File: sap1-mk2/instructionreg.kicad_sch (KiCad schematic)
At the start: 0 parts

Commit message: added A Register, B Register, Instruction Register, and Memory Address Register
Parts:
- added C18, C19, C20: 0.1μF, symbol Device:C_Small
- added D18, D19, D20, D21: BLUE, symbol Device:LED
- added D22, D23, D24, D25: YELLOW, symbol Device:LED
- added R24, R25, R26, R27, R28, R29, R30, R31: 220, symbol Device:R
- added U13: 74LS245, symbol 74xx:74LS245
- added U14, U15: 74LS173, symbol 74xx:74LS173
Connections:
- new net: D21.1 (K), R27.1
- new net: D21.2 (A), U13.2 (A0), U15.3 (Q0)
- new net: D20.2 (A), U13.3 (A1), U15.4 (Q1)
- new net: D19.2 (A), U13.4 (A2), U15.5 (Q2)
- new net: D18.2 (A), U13.5 (A3), U15.6 (Q3)
- new net: D18.1 (K), R24.1
- new net: D22.1 (K), R28.1
- new net: D25.1 (K), R31.1
- new net: D19.1 (K), R25.1
- new net: D24.1 (K), R30.1
- new net: D23.1 (K), R29.1
- new net: D20.1 (K), R26.1
- new net +5V: C18.2, C19.2, C20.2, U13.1 (A->B), U13.20 (VCC), U14.16 (VCC), U15.16 (VCC)
- new net BUS_0: U13.11 (B7), U15.11 (D3)
- new net BUS_1: U13.12 (B6), U15.12 (D2)
- new net BUS_2: U13.13 (B5), U15.13 (D1)
- new net BUS_3: U13.14 (B4), U15.14 (D0)
- new net BUS_4: U13.15 (B3), U14.11 (D3)
- new net BUS_5: U13.16 (B2), U14.12 (D2)
- new net BUS_6: U13.17 (B1), U14.13 (D1)
- new net BUS_7: U13.18 (B0), U14.14 (D0)
- new net CLK: U14.7 (Cp), U15.7 (Cp)
- new net CLR: U14.15 (Mr), U15.15 (Mr)
- new net GND: C18.1, C19.1, C20.1, R24.2, R25.2, R26.2, R27.2, R28.2, R29.2, R30.2, R31.2, U13.10 (GND), U13.6 (A4), U13.7 (A5), U13.8 (A6), U13.9 (A7), U14.1 (Oe1), U14.2 (Oe2), U14.8 (GND), U15.1 (Oe1), U15.2 (Oe2), U15.8 (GND)
- new net IR_4: D25.2 (A), U14.3 (Q0)
- new net IR_5: D24.2 (A), U14.4 (Q1)
- new net IR_6: D23.2 (A), U14.5 (Q2)
- new net IR_7: D22.2 (A), U14.6 (Q3)
- new net ~{II}: U14.10 (E2), U14.9 (E1), U15.10 (E2), U15.9 (E1)
- new net ~{IO}: U13.19 (CE)
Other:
- title: (none) -> Instruction Register

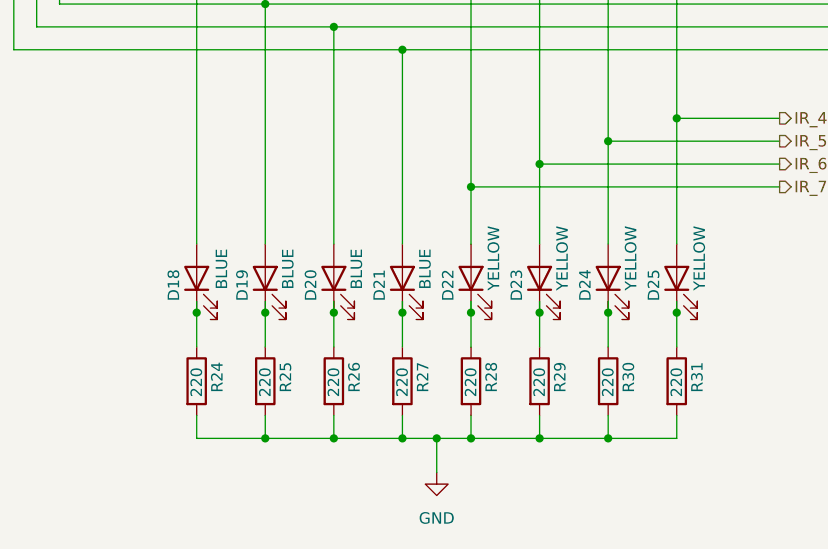
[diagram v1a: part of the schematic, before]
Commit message: added ALU + some minor tweaks
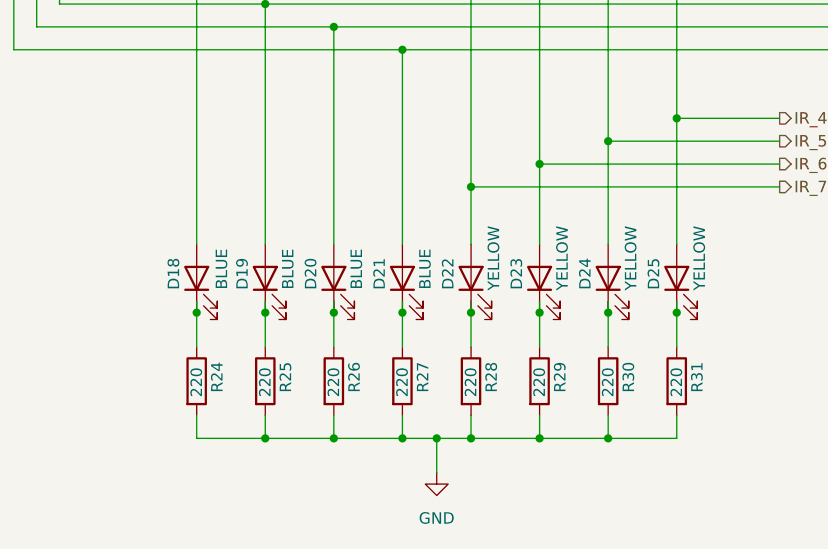
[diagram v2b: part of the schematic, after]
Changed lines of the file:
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@@
 		(dnp no)
 		(property "Reference" "D25"
-			(at 138.43 161.544 0)
+			(at 138.43 160.274 0)
 			(show_name no)
 			(do_not_autoplace no)
@@
 		(dnp no)
 		(property "Reference" "D21"
-			(at 107.95 161.544 0)
+			(at 107.95 160.274 0)
 			(show_name no)
 			(do_not_autoplace no)
@@
 		(dnp no)
 		(property "Reference" "D18"
-			(at 85.09 161.544 0)
+			(at 85.09 160.274 0)
 			(show_name no)
 			(do_not_autoplace no)
@@
 		(dnp no)
 		(property "Reference" "D23"
-			(at 123.19 161.544 0)
+			(at 123.19 160.274 0)
 			(show_name no)
 			(do_not_autoplace no)
@@
 		(dnp no)
 		(property "Reference" "D22"
-			(at 115.57 161.544 0)
+			(at 115.57 160.274 0)
 			(show_name no)
 			(do_not_autoplace no)
@@
 		(dnp no)
 		(property "Reference" "D24"
-			(at 130.81 161.544 0)
+			(at 130.81 160.274 0)
 			(show_name no)
 			(do_not_autoplace no)
@@
 		(dnp no)
 		(property "Reference" "D20"
-			(at 100.33 161.544 0)
+			(at 100.33 160.274 0)
 			(show_name no)
 			(do_not_autoplace no)
@@
 		(dnp no)
 		(property "Reference" "D19"
-			(at 92.71 161.544 0)
-			(show_name no)
-			(do_not_autoplace no)
+			(at 92.71 160.274 0)
+			(show_name no)
+			(do_not_autoplace no)
